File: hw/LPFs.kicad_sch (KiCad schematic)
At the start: 21 parts, among them U201 AS183-92LF, U202 AS183-92LF, U203 AS183-92LF, U204 AS183-92LF

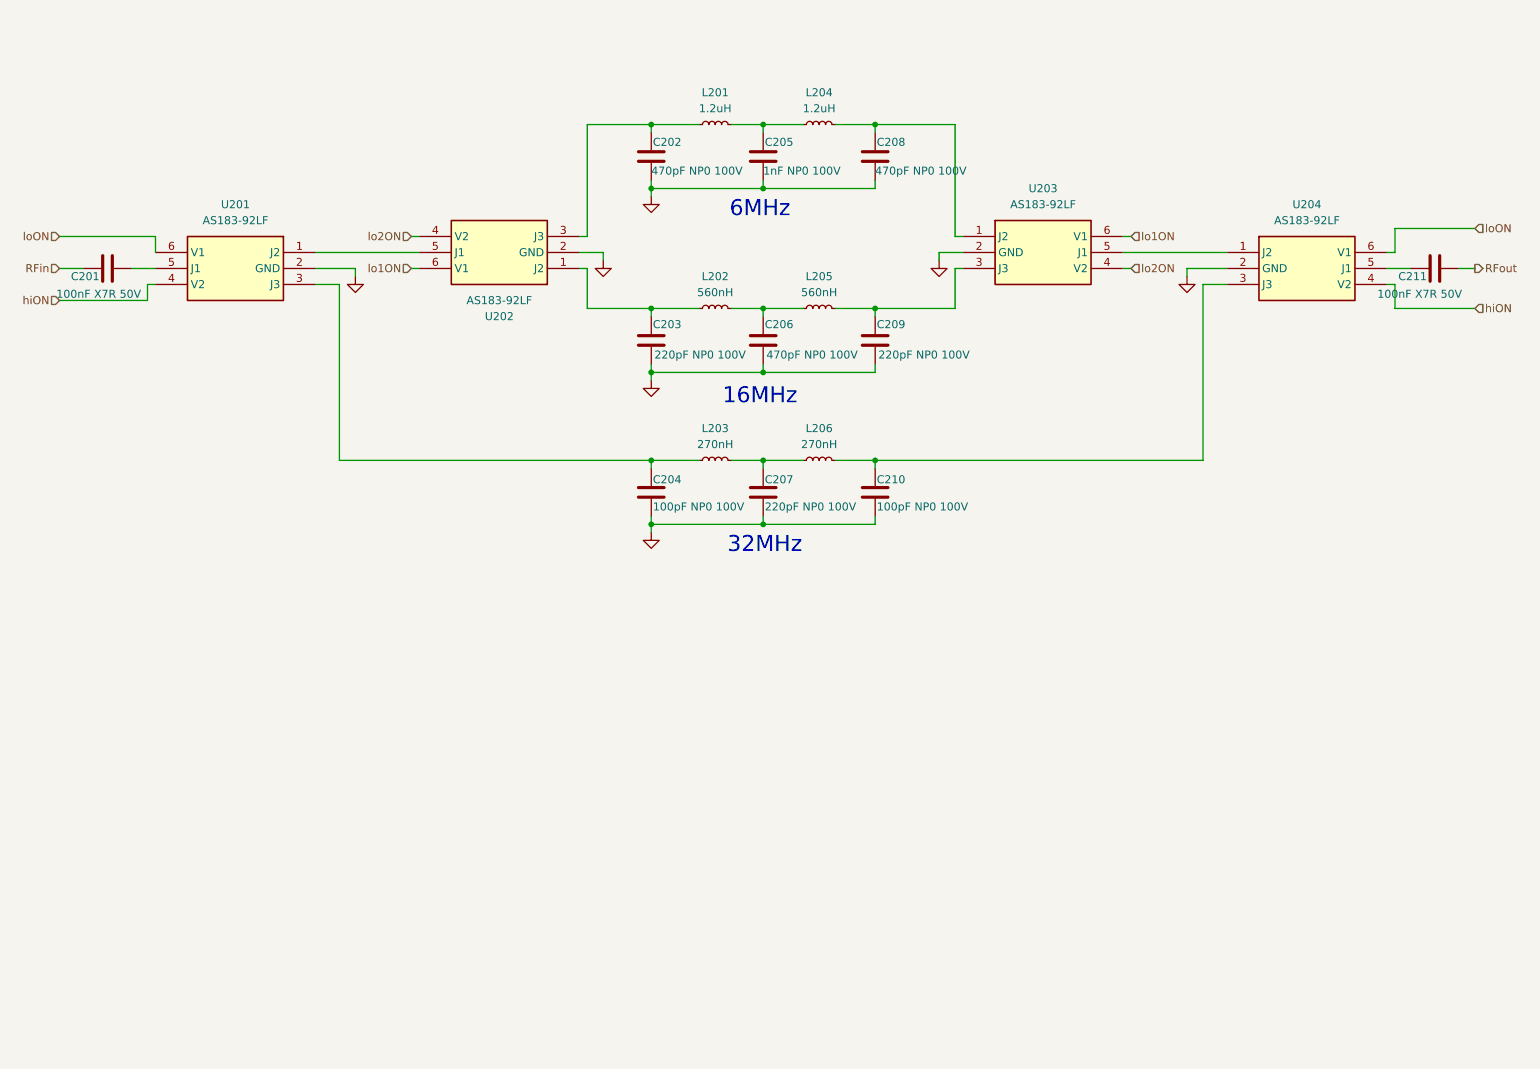
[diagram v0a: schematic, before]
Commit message: Use relays and do layout over again to make these damned things fit
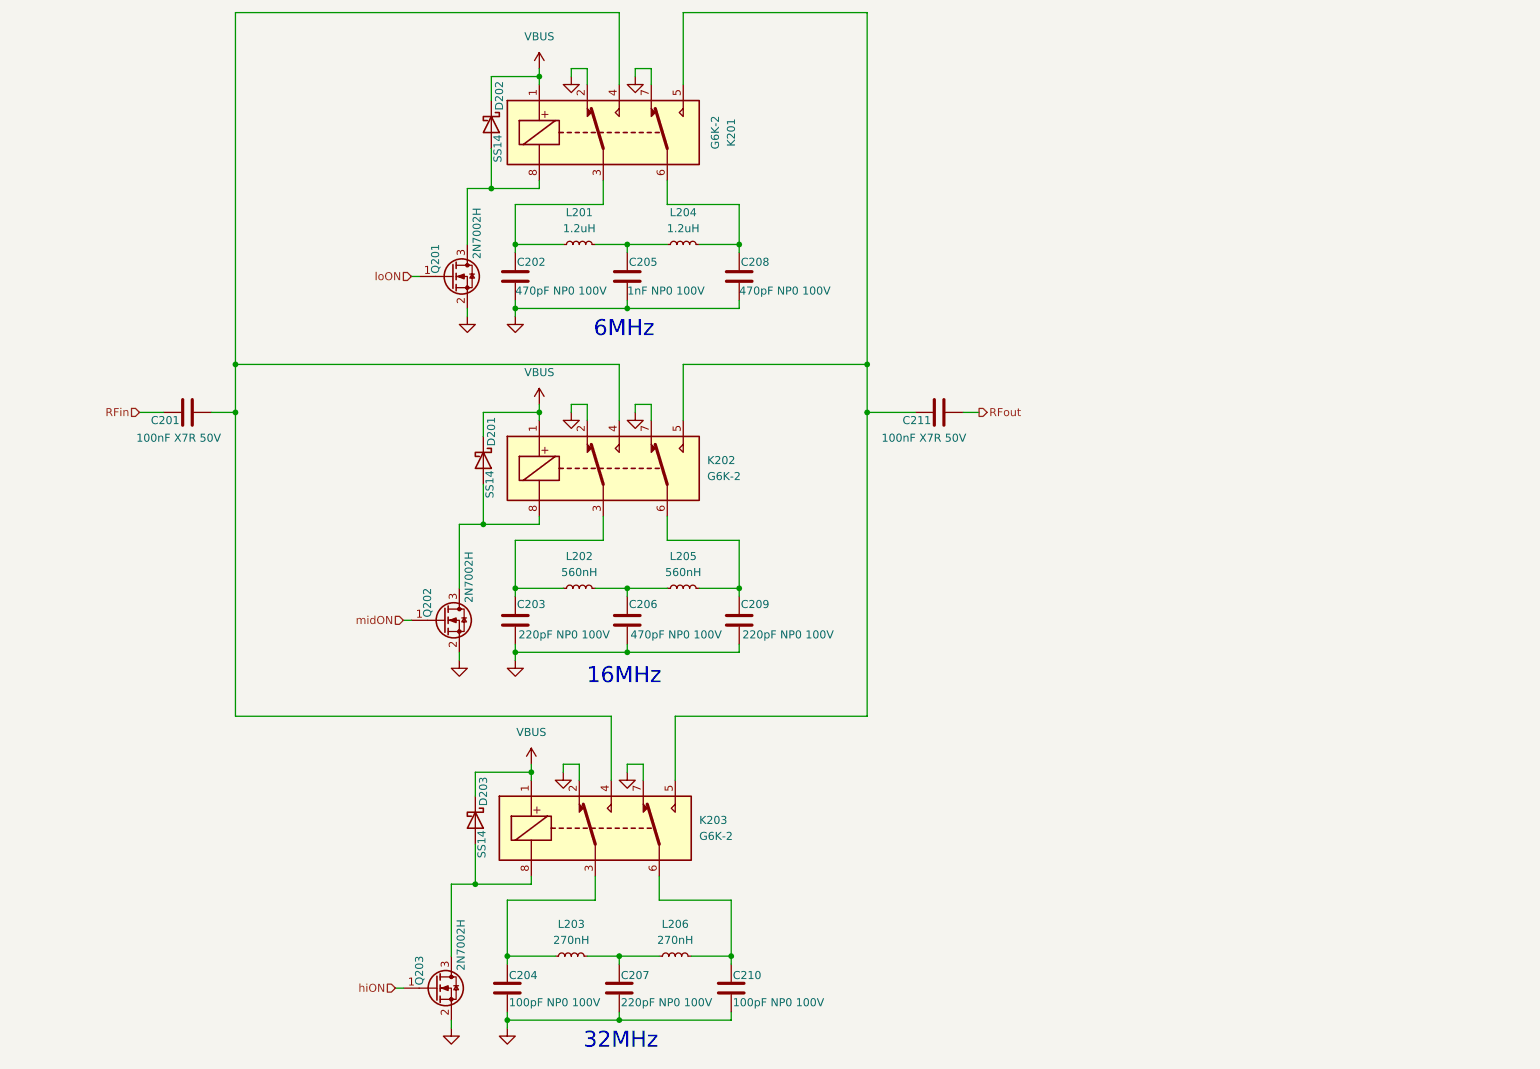
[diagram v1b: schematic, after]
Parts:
- removed U201, U202, U203, U204: AS183-92LF, Library:SOT65P220X110-6N, symbol Library:AS183-92LF
- added D201, D202, D203: SS14, Diode_SMD:D_SMA, symbol Diode:SS14
- added K201, K202, K203: G6K-2, Relay_SMD:Relay_DPDT_Omron_G6K-2G, symbol Relay:G6K-2
- added Q201, Q202, Q203: 2N7002H, Package_TO_SOT_SMD:SOT-23, symbol Transistor_FET:2N7002H
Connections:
- net GND: now also K201.2, K201.7, K202.2, K202.7, K203.2, K203.7, Q201.2 (S), Q202.2 (S), Q203.2 (S)
- net hiON: now also Q203.1 (G)
- net loON: now also Q201.1 (G)
- net at C208.1, L204.2: now also K201.6
- net at C210.1, L206.2: now also K203.6
- net at C211.1: now also K201.5, K202.5, K203.5
- net at C204.1, L203.1: now also K203.3
- net at C209.1, L205.2: now also K202.6
- net at C202.1, L201.1: now also K201.3
- net at C201.2: now also K201.4, K202.4, K203.4
- net at C203.1, L202.1: now also K202.3
- new net: D201.2 (A), K202.8, Q202.3 (D)
- new net: D202.2 (A), K201.8, Q201.3 (D)
- new net: D203.2 (A), K203.8, Q203.3 (D)
- new net VBUS: D201.1 (K), D202.1 (K), D203.1 (K), K201.1, K202.1, K203.1
- new net midON: Q202.1 (G)
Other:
- moved on the sheet: C201, C202, C203, C204, C205, C206, C207, C208, C209, C210, C211, L201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
